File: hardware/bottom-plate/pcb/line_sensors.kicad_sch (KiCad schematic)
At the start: 99 parts

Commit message: bottom plate schematic, and removed some random stuff
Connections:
- net AMUX2_EN is gone; now on net AMUX_EN: AMUX2.15 (~{E})
- net AMUX3_EN is gone; now on net AMUX_EN: AMUX3.15 (~{E})
- net +3.3V renamed +3V3
- net AMUX1_EN renamed AMUX_EN
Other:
- added sheet LEDs (LEDs.kicad_sch)
- moved on the sheet: PR1, PR10, PR11, PR12, PR13, PR14, PR15, PR16, PR17, PR18, PR19, PR2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

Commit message: kicker pcb done, working on bottom plate
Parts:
- R1, R10, R11, R12, R13, R14, R15, R16, R17, R18, R19, R2, R20, R21, R22, R23, R24, R25, R26, R27, R28, R29, R3, R30, R31, R32, R33, R34, R35, R36, R37, R38, R39, R4, R40, R41, R42, R43, R44, R45, R46, R47, R48, R5, R6, R7, R8, R9: footprint PCM_Resistor_SMD_AKL:R_0603_1608Metric_Pad0.98x0.95mm_HandSolder -> PCM_Resistor_SMD_AKL:R_0805_2012Metric_Pad1.15x1.40mm_HandSolder

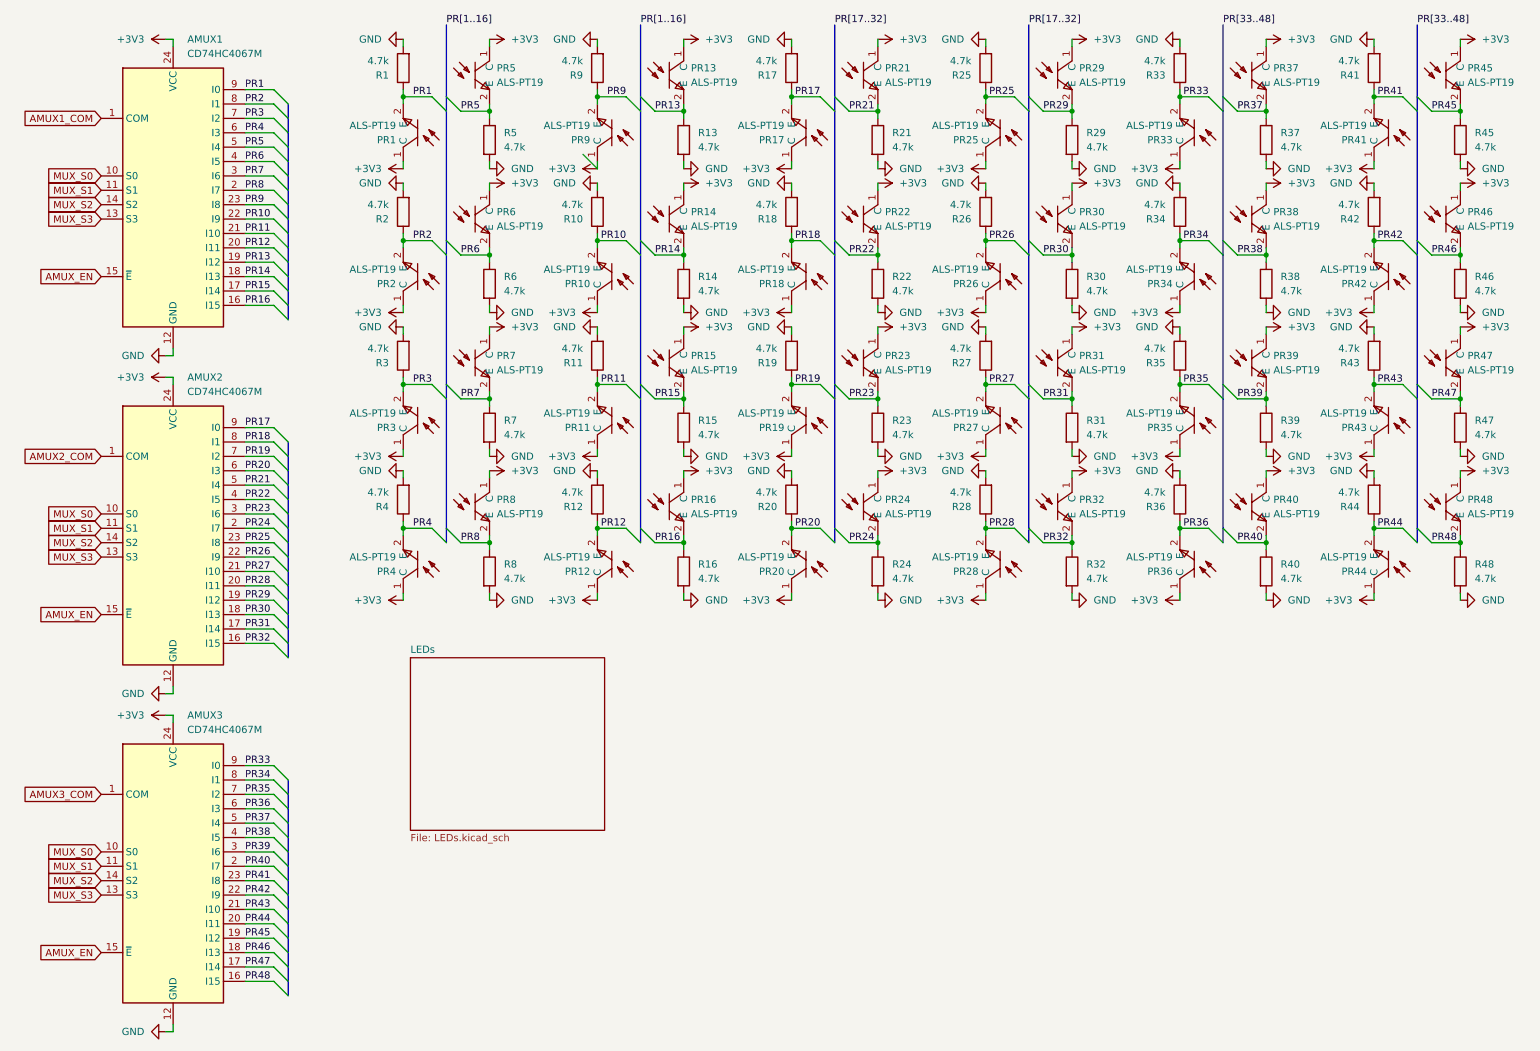
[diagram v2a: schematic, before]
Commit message: cleaned up bottom plate schematic and added explanations of design decisions. Please read.
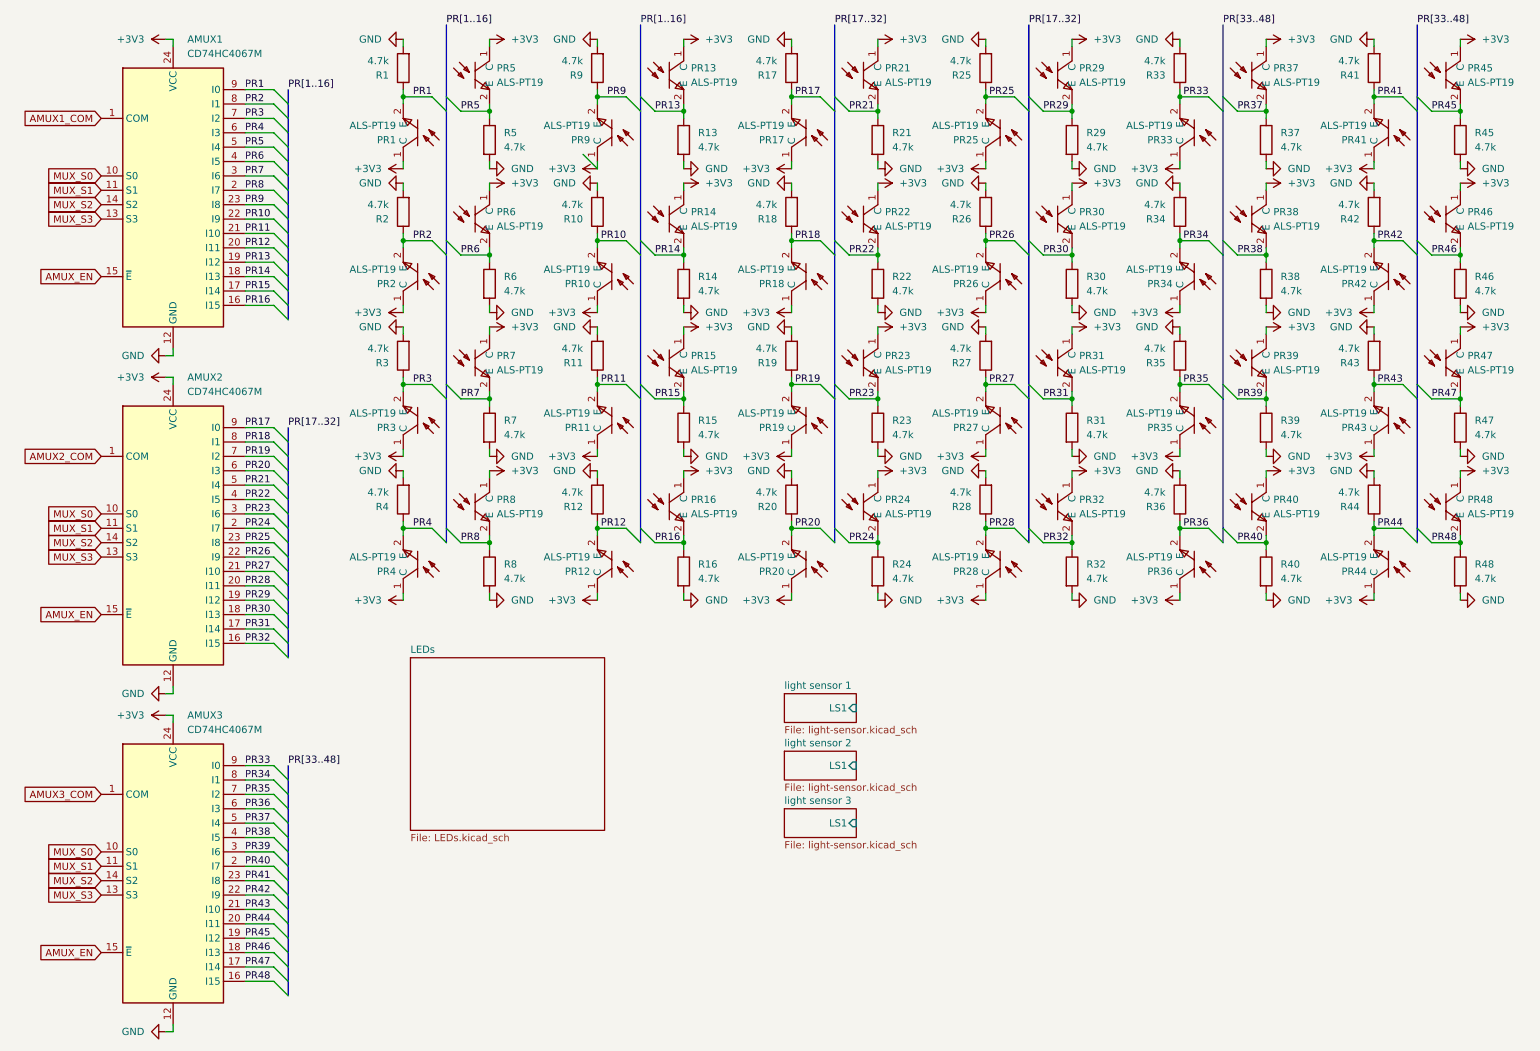
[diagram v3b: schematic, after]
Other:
- added sheet light sensor 1 (light-sensor.kicad_sch)
- added sheet light sensor 2 (light-sensor.kicad_sch)
- added sheet light sensor 3 (light-sensor.kicad_sch)
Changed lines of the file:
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@@
 	(bus
 		(pts
+			(xy 62.23 86.36) (xy 62.23 88.9)
+		)
+		(stroke
+			(width 0)
+			(type default)
+		)
+	)
+	(bus
+		(pts
 			(xy 62.23 109.22) (xy 62.23 111.76)
 		)
@@
 	(bus
 		(pts
+			(xy 62.23 146.05) (xy 62.23 148.59)
+		)
+		(stroke
+			(width 0)
+			(type default)
+		)
+	)
+	(bus
+		(pts
 			(xy 62.23 176.53) (xy 62.23 179.07)
 		)
@@
 	(bus
 		(pts
+			(xy 62.23 26.67) (xy 62.23 29.21)
+		)
+		(stroke
+			(width 0)
+			(type default)
+		)
+	)
+	(bus
+		(pts
 			(xy 62.23 34.29) (xy 62.23 36.83)
 		)
@@
 		)
 	)
+	(label "PR[1..16]"
+		(at 62.23 26.67 0)
+		(fields_autoplaced yes)
+		(effects
+			(font
+				(size 1.27 1.27)
+			)
+			(justify left bottom)
+		)
+	)
 	(label "PR42"
 		(at 54.61 168.91 0)
@@
 		)
 	)
+	(label "PR[17..32]"
+		(at 62.23 86.36 0)
+		(fields_autoplaced yes)
+		(effects
+			(font
+				(size 1.27 1.27)
+			)
+			(justify left bottom)
+		)
+	)
 	(label "PR33"
 		(at 54.61 146.05 0)
@@
 		)
 	)
+	(label "PR[33..48]"
+		(at 62.23 146.05 0)
+		(fields_autoplaced yes)
+		(effects
+			(font
+				(size 1.27 1.27)
+			)
+			(justify left bottom)
+		)
+	)
 	(label "PR46"
 		(at 54.61 179.07 0)
@@
 				)
 			)
+		)
+	)
+	(sheet
+		(at 149.86 133.35)
+		(size 12.7 5.08)
+		(fields_autoplaced yes)
+		(stroke
+			(width 0.1524)
+			(type solid)
+		)
+		(fill
+			(color 0 0 0 0.0000)
+		)
+		(property "Sheetname" "light sensor 1"
+			(at 149.86 132.6384 0)
+			(effects
+				(font
+					(size 1.27 1.27)
+				)
+				(justify left bottom)
+			)
+		)
+		(property "Sheetfile" "light-sensor.kicad_sch"
+			(at 149.86 139.0146 0)
+			(effects
+				(font
+					(size 1.27 1.27)
+				)
+				(justify left top)
+			)
+		)
+		(property "Field2" ""
+			(at 149.86 133.35 0)
+			(effects
+				(font
+					(size 1.27 1.27)
+				)
+				(hide yes)
+			)
+		)
+		(pin "LS1" input
+			(at 162.56 135.89 0)
+			(effects
+				(font
+					(size 1.27 1.27)
+				)
+				(justify right)
+			)
+		)
+		(instances
+			(project "pcb"
+				(path "/7e6d4b79-c480-4b70-bccc-d28260cddf7c/8e7ff108-03cd-4ca5-8da7-ac905b14624c"
+					(page "5")
+				)
+			)
+		)
+	)
+	(sheet
+		(at 149.86 143.51)
+		(size 12.7 5.08)
+		(fields_autoplaced yes)
+		(stroke
+			(width 0.1524)
+			(type solid)
+		)
+		(fill
+			(color 0 0 0 0.0000)
+		)
+		(property "Sheetname" "light sensor 2"
+			(at 149.86 142.7984 0)
+			(effects
+				(font
+					(size 1.27 1.27)
+				)
+				(justify left bottom)
+			)
+		)
+		(property "Sheetfile" "light-sensor.kicad_sch"
+			(at 149.86 149.1746 0)
+			(effects
+				(font
+					(size 1.27 1.27)
+				)
+				(justify left top)
+			)
+		)
+		(property "Field2" ""
+			(at 149.86 143.51 0)
+			(effects
+				(font
+					(size 1.27 1.27)
+				)
+				(hide yes)
+			)
+		)
+		(pin "LS1" input
+			(at 162.56 146.05 0)
+			(effects
+				(font
+					(size 1.27 1.27)
+				)
+				(justify right)
+			)
+		)
+		(instances
+			(project "pcb"
+				(path "/7e6d4b79-c480-4b70-bccc-d28260cddf7c/8e7ff108-03cd-4ca5-8da7-ac905b14624c"
+					(page "6")
+				)
+			)
+		)
+	)
+	(sheet
+		(at 149.86 153.67)
+		(size 12.7 5.08)
+		(fields_autoplaced yes)
+		(stroke
+			(width 0.1524)
+			(type solid)
+		)
+		(fill
+			(color 0 0 0 0.0000)
+		)
+		(property "Sheetname" "light sensor 3"
+			(at 149.86 152.9584 0)
+			(effects
+				(font
+					(size 1.27 1.27)
+				)
+				(justify left bottom)
+			)
+		)
+		(property "Sheetfile" "light-sensor.kicad_sch"
+			(at 149.86 159.3346 0)
+			(effects
+				(font
+					(size 1.27 1.27)
+				)
+				(justify left top)
+			)
+		)
+		(property "Field2" ""
+			(at 149.86 153.67 0)
+			(effects
+				(font
+					(size 1.27 1.27)
+				)
+				(hide yes)
+			)
+		)
+		(pin "LS1" input
+			(at 162.56 156.21 0)
+			(effects
+				(font
+					(size 1.27 1.27)
+				)
+				(justify right)
+			)
+		)
+		(instances
+			(project "pcb"
+				(path "/7e6d4b79-c480-4b70-bccc-d28260cddf7c/8e7ff108-03cd-4ca5-8da7-ac905b14624c"
+					(page "7")
+				)
+			)
